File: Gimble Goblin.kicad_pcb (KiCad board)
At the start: 2 copper layers, 14 parts, among them J1 RJ45_LED_Shielded, J2 CONN_03, J3 CONN_03, J4 CONN_03, U1 L7805, U2 MCP2515-EST, U3 ATA6560,1, Y1 20MHz

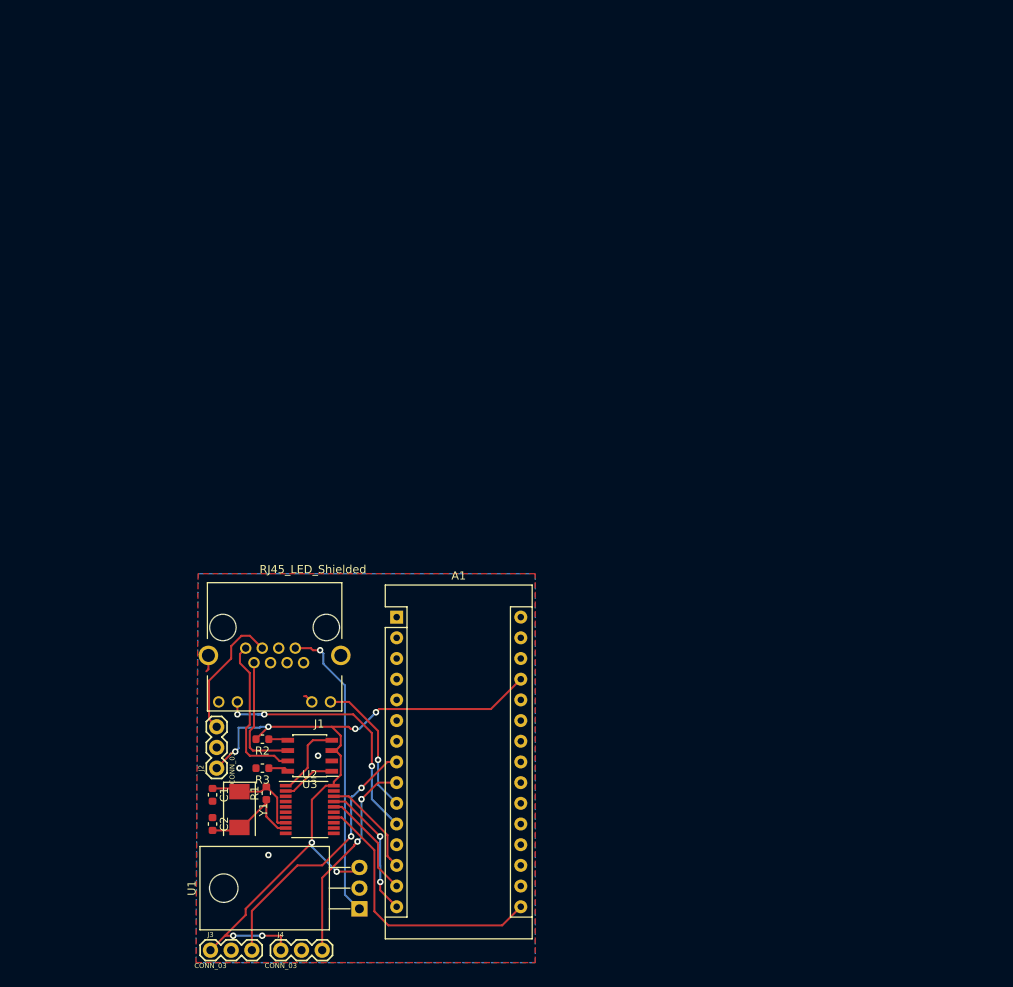
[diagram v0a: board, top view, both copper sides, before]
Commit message: Re-organized schematic
Fixed schematic,
Updated PCB and compomnents
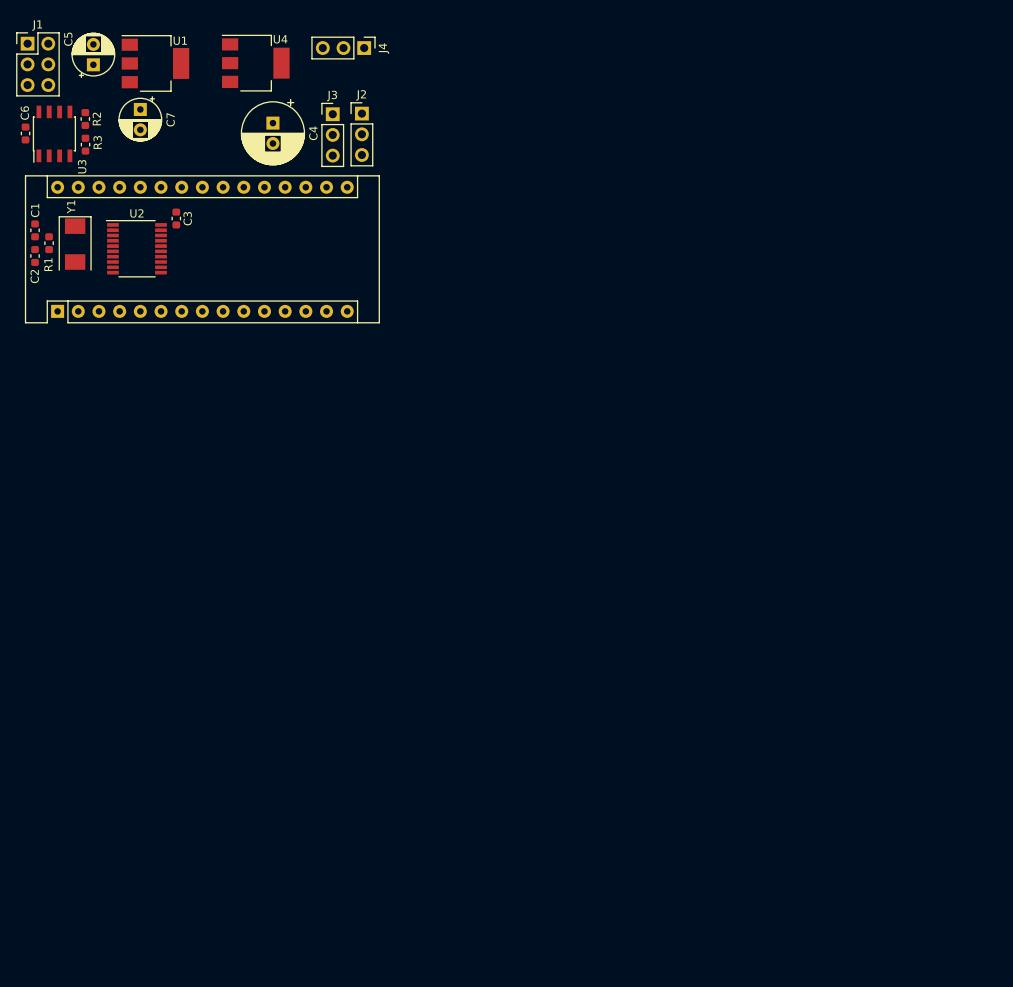
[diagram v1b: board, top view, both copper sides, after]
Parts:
- added C3: 0.1uF, Capacitor_SMD:C_0603_1608Metric, F.Cu at (53.0, 43.3)
- added C4: 220uF, Capacitor_THT:CP_Radial_D7.5mm_P2.50mm, F.Cu at (64.8, 31.5)
- added C5: 100uF, Capacitor_THT:CP_Radial_D5.0mm_P2.50mm, F.Cu at (42.8, 24.4)
- added C6: 0.1uF, Capacitor_SMD:C_0603_1608Metric, F.Cu at (34.4, 32.8)
- added C7: 100uF, Capacitor_THT:CP_Radial_D5.0mm_P2.50mm, F.Cu at (48.5, 29.9)
- added U4: L7805, Package_TO_SOT_SMD:SOT-223, F.Cu at (62.7, 24.2)
- J1: value RJ45_LED_Shielded -> Conn_02x03_Odd_Even; footprint RJHSE-5381:AMPHENOL_RJHSE-5381 -> Connector_PinHeader_2.54mm:PinHeader_2x03_P2.54mm_Vertical
- J2, J3, J4: value CONN_03 -> Conn_01x03_Male; footprint Connectors:1X03 -> Connector_PinHeader_2.54mm:PinHeader_1x03_P2.54mm_Vertical
- U1: footprint Package_TO_SOT_THT:TO-220-3_Horizontal_TabDown -> Package_TO_SOT_SMD:SOT-223
- moved J4 111.2 mm to (76.0, 22.3), turned to 270 degrees
- moved U1 106.8 mm to (50.4, 24.2), turned to 0 degrees
- moved J3 103.7 mm to (72.2, 30.5)
- moved U3 82.5 mm to (38.0, 32.9), turned to 90 degrees
- moved J2 82.3 mm to (75.7, 30.4), turned to 0 degrees
- moved R3 79.6 mm to (41.8, 34.2), turned to 270 degrees
- moved R2 79.2 mm to (41.8, 31.0), turned to 90 degrees
- moved J1 77.8 mm to (34.7, 21.8), turned to 0 degrees
- moved C2 73.1 mm to (35.6, 47.9), turned to 90 degrees
- moved C1 72.7 mm to (35.6, 44.7), turned to 90 degrees
- moved R1 72.6 mm to (37.3, 46.3)
- moved Y1 72.3 mm to (40.5, 46.4)
- moved U2 72.0 mm to (48.1, 47.0)
- moved A1 56.1 mm to (38.4, 54.7), turned to 90 degrees
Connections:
- net Net-(A1-Pad14) renamed MOSI
- net Net-(A1-Pad15) renamed MISO
- net Net-(A1-Pad16) renamed SCK
- A1 pad 19: Net-(A1-Pad19) -> nCS
- A1 pad 27: Net-(A1-Pad27) -> +5V
- A1 pad 5: Net-(A1-Pad5) -> INT
- A1 pad 6: Net-(A1-Pad6) -> RX0
- A1 pad 8: Net-(A1-Pad8) -> Gx
- A1 pad 9: Net-(A1-Pad9) -> Gy
- J1 pad 1: CANH -> CAM
- J1 pad 2: CANL -> +12V
- J1 pad 3: Net-(J1-Pad3) -> GND
- J1 pad 4: Net-(J1-Pad4) -> GND
- J1 pad 5: Net-(J1-Pad5) -> CANH
- J1 pad 6: Net-(J1-Pad6) -> CANL
- J2 pad 1: Net-(A1-Pad27) -> GND
- J2 pad 2: GND -> +5VA
- J2 pad 3: Net-(J1-Pad3) -> Gx
- J3 pad 1: Net-(A1-Pad27) -> GND
- J3 pad 2: GND -> +5VA
- J3 pad 3: Net-(A1-Pad8) -> Gy
- J4 pad 1: Net-(A1-Pad27) -> GND
- J4 pad 2: GND -> +5V
- J4 pad 3: Net-(A1-Pad9) -> CAM
- R2 pad 1: Net-(R2-Pad1) -> +5V
- R2 pad 2: Net-(A1-Pad27) -> Net-(R2-Pad2)
- U1 pad 1: Net-(J1-Pad7) -> +12V
- U1 pad 3: Net-(A1-Pad27) -> +5VA
- U2 pad 1: Net-(U2-Pad1) -> C_TX
- U2 pad 18: Net-(A1-Pad13) -> nCS
- U2 pad 2: Net-(U2-Pad2) -> C_RX
- U2 pad 20: Net-(A1-Pad27) -> +5V
- U3 pad 1: Net-(U2-Pad2) -> C_TX
- U3 pad 3: Net-(A1-Pad27) -> +5V
- U3 pad 4: Net-(U2-Pad1) -> C_RX
- U3 pad 5: Net-(R2-Pad1) -> Net-(R2-Pad2)
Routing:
- net Net-(A1-Pad27): track 98.3 -> 0.00 mm, vias 8 -> 0
- net Net-(J1-Pad7): track 36.9 -> 0.00 mm, vias 1 -> 0
- net SCK: track 33.8 -> 0.00 mm
- net Net-(A1-Pad8): track 33.0 -> 0.00 mm, vias 2 -> 0
- net Net-(A1-Pad11): track 31.9 -> 0.00 mm, vias 3 -> 0
- net Net-(A1-Pad9): track 25.7 -> 0.00 mm, vias 2 -> 0
- net CANH: track 19.8 -> 0.00 mm
- net Net-(A1-Pad10): track 17.2 -> 0.00 mm, vias 1 -> 0
- net MISO: track 17.0 -> 0.00 mm, vias 2 -> 0
- net Net-(J1-Pad3): track 16.4 -> 0.00 mm
- net CANL: track 15.5 -> 0.00 mm
- net MOSI: track 13.5 -> 0.00 mm
- net Net-(C2-Pad2): track 13.5 -> 0.00 mm
- net Net-(C1-Pad1): track 13.3 -> 0.00 mm
- net Net-(A1-Pad13): track 12.8 -> 0.00 mm
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- removed copper zone on B.Cu, net GND
- removed copper zone on F.Cu, net GND
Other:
- rule pad_to_mask_clearance: 0.2 -> 0

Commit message: Routed PCB
Worked on silkscreen
Finished all routing and via stiching
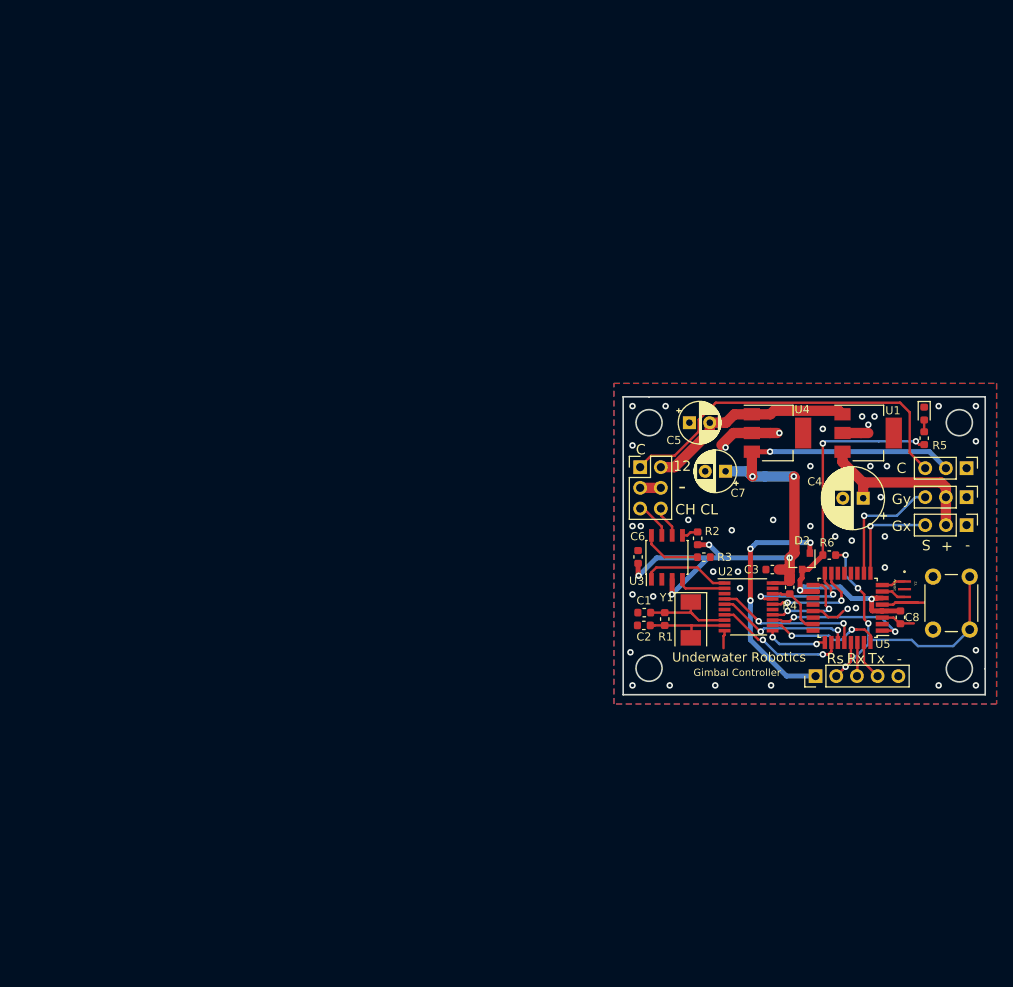
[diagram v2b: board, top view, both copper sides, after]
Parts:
- removed A1: Arduino_Nano_v3.x, Module:Arduino_Nano
- added C8: 0.1uF, Capacitor_SMD:C_0603_1608Metric, F.Cu at (141.9, 92.2)
- added D1: LED, LED_SMD:LED_0603_1608Metric, F.Cu at (144.8, 67.2)
- added D2: D_x2_KCom_AAK, Package_TO_SOT_SMD:SOT-23, F.Cu at (129.8, 85.3)
- added J5: PROG, Connector_PinHeader_2.54mm:PinHeader_1x05_P2.54mm_Vertical, F.Cu at (131.4, 99.4)
- added R4: 10k, Resistor_SMD:R_0603_1608Metric, F.Cu at (128.3, 88.5)
- added R5: 330, Resistor_SMD:R_0603_1608Metric, F.Cu at (144.8, 70.2)
- added R6: 10k, Resistor_SMD:R_0603_1608Metric, F.Cu at (133.1, 84.6)
- added SW1: SW_Push, Button_Switch_THT:SW_PUSH_6mm, F.Cu at (150.4, 87.2)
- added U5: ATmega328P-AU, Package_QFP:TQFP-32_7x7mm_P0.8mm, F.Cu at (135.4, 91.1)
- added Y2: 16MHz, CSTCE16M0V53-R0:OSC_CSTCE16M0V53-R0, F.Cu at (142.4, 88.8)
- moved U1 98.6 mm to (137.9, 69.6)
- moved J3 92.7 mm to (150.0, 80.9), turned to 270 degrees
- moved J1 91.4 mm to (109.9, 73.8)
- moved U3 91.4 mm to (113.2, 84.9)
- moved C6 91.4 mm to (109.7, 84.8)
- moved R3 91.3 mm to (117.7, 84.8), turned to 0 degrees
- moved R2 91.1 mm to (117.0, 82.5)
- moved J4 90.2 mm to (150.0, 73.9)
- moved R1 88.6 mm to (112.9, 92.4)
- moved Y1 88.6 mm to (116.1, 92.5)
- moved C1 88.3 mm to (110.4, 91.6), turned to 180 degrees
- moved J2 87.9 mm to (150.0, 77.5), turned to 270 degrees
- moved C2 87.4 mm to (110.4, 93.2), turned to 0 degrees
- moved U2 87.0 mm to (123.2, 90.9)
- moved C4 85.9 mm to (137.3, 77.6), turned to 180 degrees
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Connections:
- J2 pad 3: Gx -> Gy
- J3 pad 3: Gy -> Gx
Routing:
- net +5V: track 0.00 -> 86.8 mm, vias 0 -> 7
- net V_MCU: track 0.00 -> 50.7 mm, vias 0 -> 4
- net CAM: track 0.00 -> 45.8 mm
- net RESET: track 0.00 -> 42.2 mm, vias 0 -> 4
- net GND: track 0.00 -> 32.1 mm, vias 0 -> 42
- net VPP: track 0.00 -> 30.0 mm, vias 0 -> 3
- net +12V: track 0.00 -> 26.2 mm
- net +5VA: track 0.00 -> 21.8 mm
- net TX0: track 0.00 -> 18.2 mm, vias 0 -> 2
- net INT: track 0.00 -> 17.7 mm, vias 0 -> 2
- net TX1: track 0.00 -> 17.1 mm, vias 0 -> 2
- net TX2: track 0.00 -> 16.4 mm, vias 0 -> 2
- net Gy: track 0.00 -> 15.5 mm, vias 0 -> 1
- net RX0: track 0.00 -> 14.6 mm, vias 0 -> 2
- net MISO: track 0.00 -> 13.6 mm, vias 0 -> 2
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- added copper zone on B.Cu, net GND
- added copper zone on F.Cu, net GND
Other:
- board outline added: 44.5 x 36.6 mm
- board text added: "+"
- board text added: "-"
- board text added: "12"
- board text added: "C"
- board text added: "CH CL"
- board text added: "Gimbal Controller"
- board text added: "Gx"
- board text added: "Gy"
- board text added: "Rs"
- board text added: "Rx"
- board text added: "S"
- board text added: "Tx"
- board text added: "Underwater Robotics"

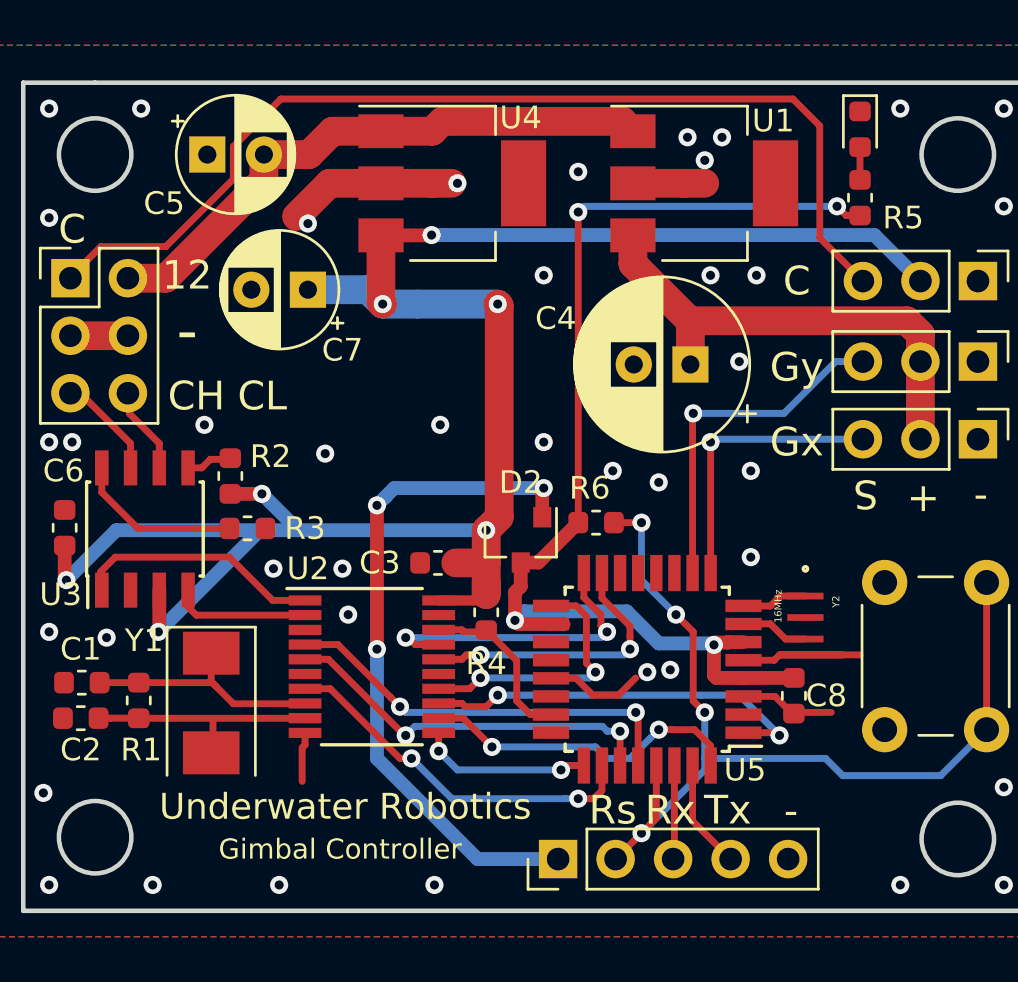
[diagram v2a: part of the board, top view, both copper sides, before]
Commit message: Implemented review fixes
Generated step file,
Generated gerber zip with drills,
Also verified gerbers online
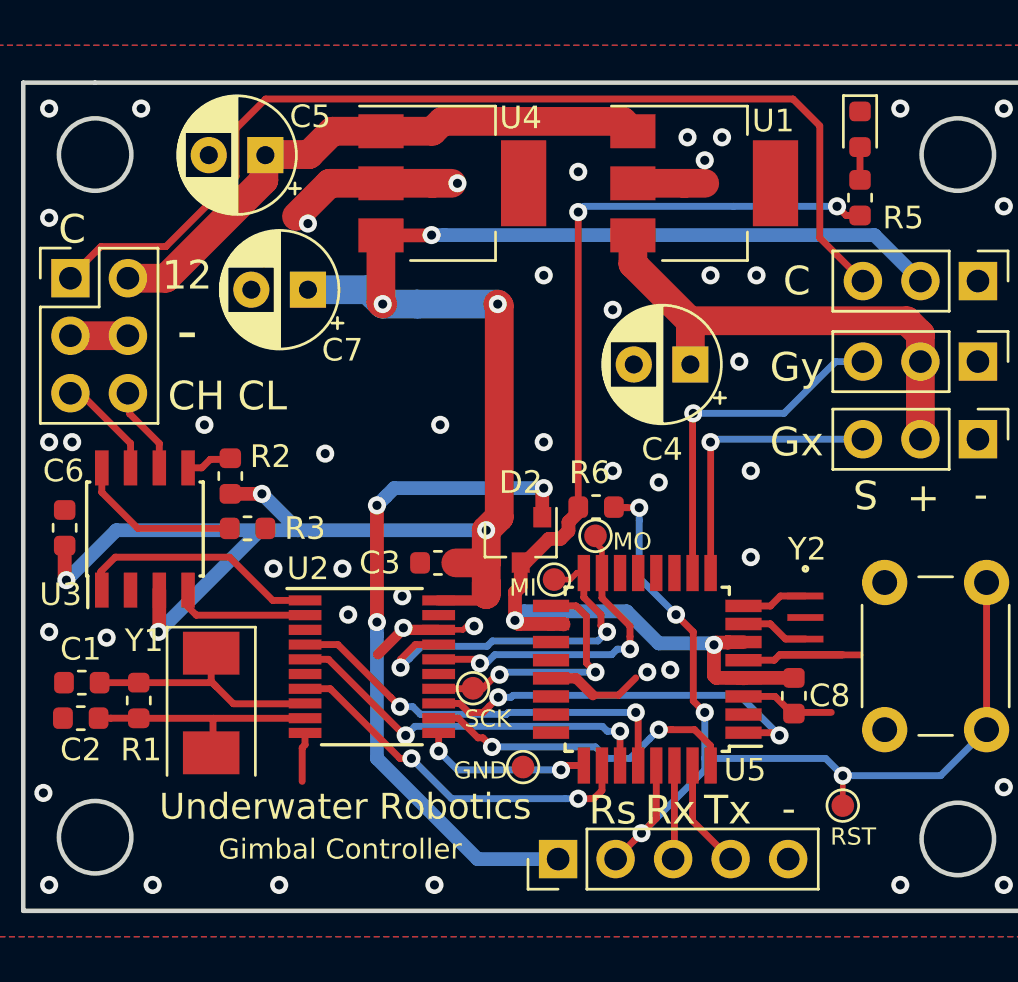
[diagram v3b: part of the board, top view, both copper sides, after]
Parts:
- removed R4: 10k, Resistor_SMD:R_0603_1608Metric
- added TP1: MOSI, TestPoint:TestPoint_Pad_D1.0mm, F.Cu at (133.1, 85.2)
- added TP2: MISO, TestPoint:TestPoint_Pad_D1.0mm, F.Cu at (131.3, 87.1)
- added TP3: SCK, TestPoint:TestPoint_Pad_D1.0mm, F.Cu at (127.7, 91.9)
- added TP4: RESET, TestPoint:TestPoint_Pad_D1.0mm, F.Cu at (144.0, 97.1)
- added TP5: GND, TestPoint:TestPoint_Pad_D1.0mm, F.Cu at (129.9, 95.4)
- C4: value 220uF -> 100uF; footprint Capacitor_THT:CP_Radial_D7.5mm_P2.50mm -> Capacitor_THT:CP_Radial_D5.0mm_P2.50mm
- moved C5 2.57 mm to (118.5, 68.4), turned to 180 degrees
- moved R6 0.69 mm to (133.1, 83.9)
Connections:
- C5 pad 1: GND -> +12V
- C5 pad 2: +12V -> GND
- U2 pad 18: nCS -> GND
- U5 pad 23: nCS -> Net-(U5-Pad23)
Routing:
- net nCS: track 7.58 -> 0.00 mm
- net GND: track 32.1 -> 36.9 mm, vias 42 -> 45
- net MISO: track 13.6 -> 16.5 mm
- net MOSI: track 12.5 -> 14.5 mm
- net RESET: track 42.2 -> 44.2 mm, vias 4 -> 5
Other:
- board text added: "GND"
- board text added: "MI"
- board text added: "MO"
- board text added: "RST"
- board text added: "SCK"
